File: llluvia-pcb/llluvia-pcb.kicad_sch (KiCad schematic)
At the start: 30 parts, among them J2 JACK_DC, J3 JACK_DC, J4 ON/OFF, J5 AudioJack, Q2 PN2222A, U1 LM324

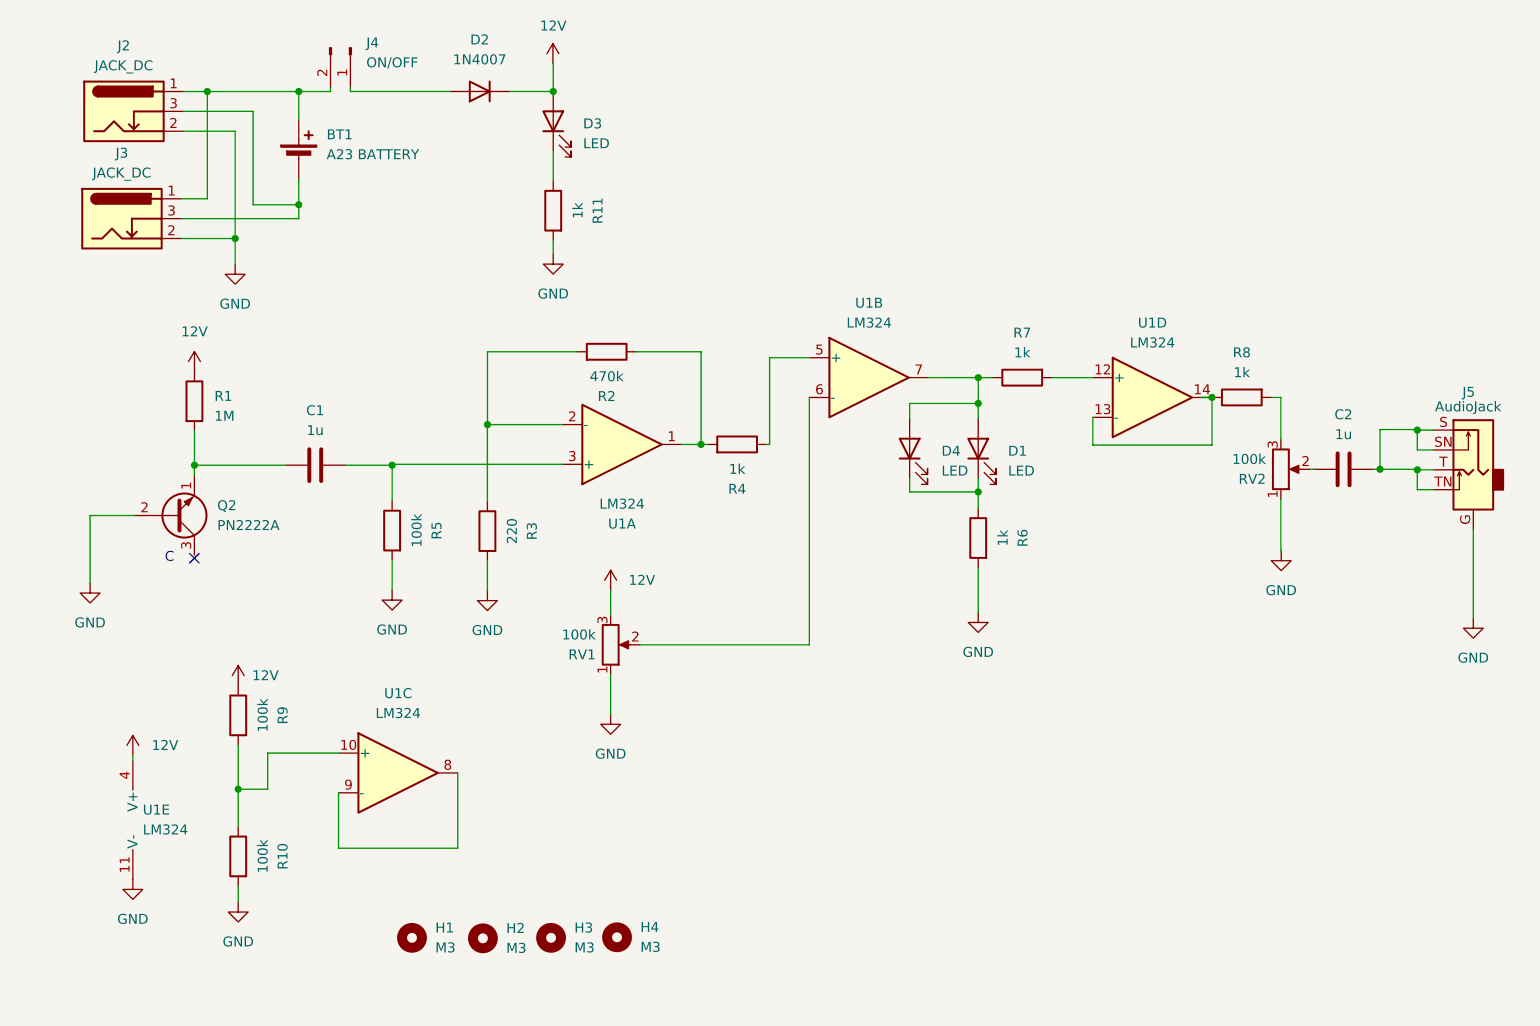
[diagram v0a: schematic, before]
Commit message: Esquemático rev 3: estabilizar etapa de ruido y comparador
- C3 (47u) en serie con R3: la ganancia DC de U1A baja de ~2137 a 1,
  así el offset y la corriente de bias del LM324 ya no lo saturan.
- R5 y extremo inferior de RV1 conectados a VREF (salida de U1C, que
  antes no iba a ningún lado). El ruido oscila alrededor de VREF y
  todo el recorrido de RV1 es útil.
- C4 (10u) en el divisor R9/R10 para filtrar VREF.
- C5 (100n) + C6 (47u) de desacople en el riel de 12V.
- R12 (100k, DNP) opcional: histéresis ~0,1 V en el comparador U1B.
- R11 1k -> 4.7k: el LED piloto pasa de ~9 mA a ~2 mA (batería A23).

El PCB no está actualizado: requiere Update PCB from Schematic y ruteo.

Co-Authored-By: Claude Opus 5.5 <noreply@anthropic.com>
Claude-Session: https://claude.ai/code/session_01RUaYEoGPN41cDPPqmjMNFH
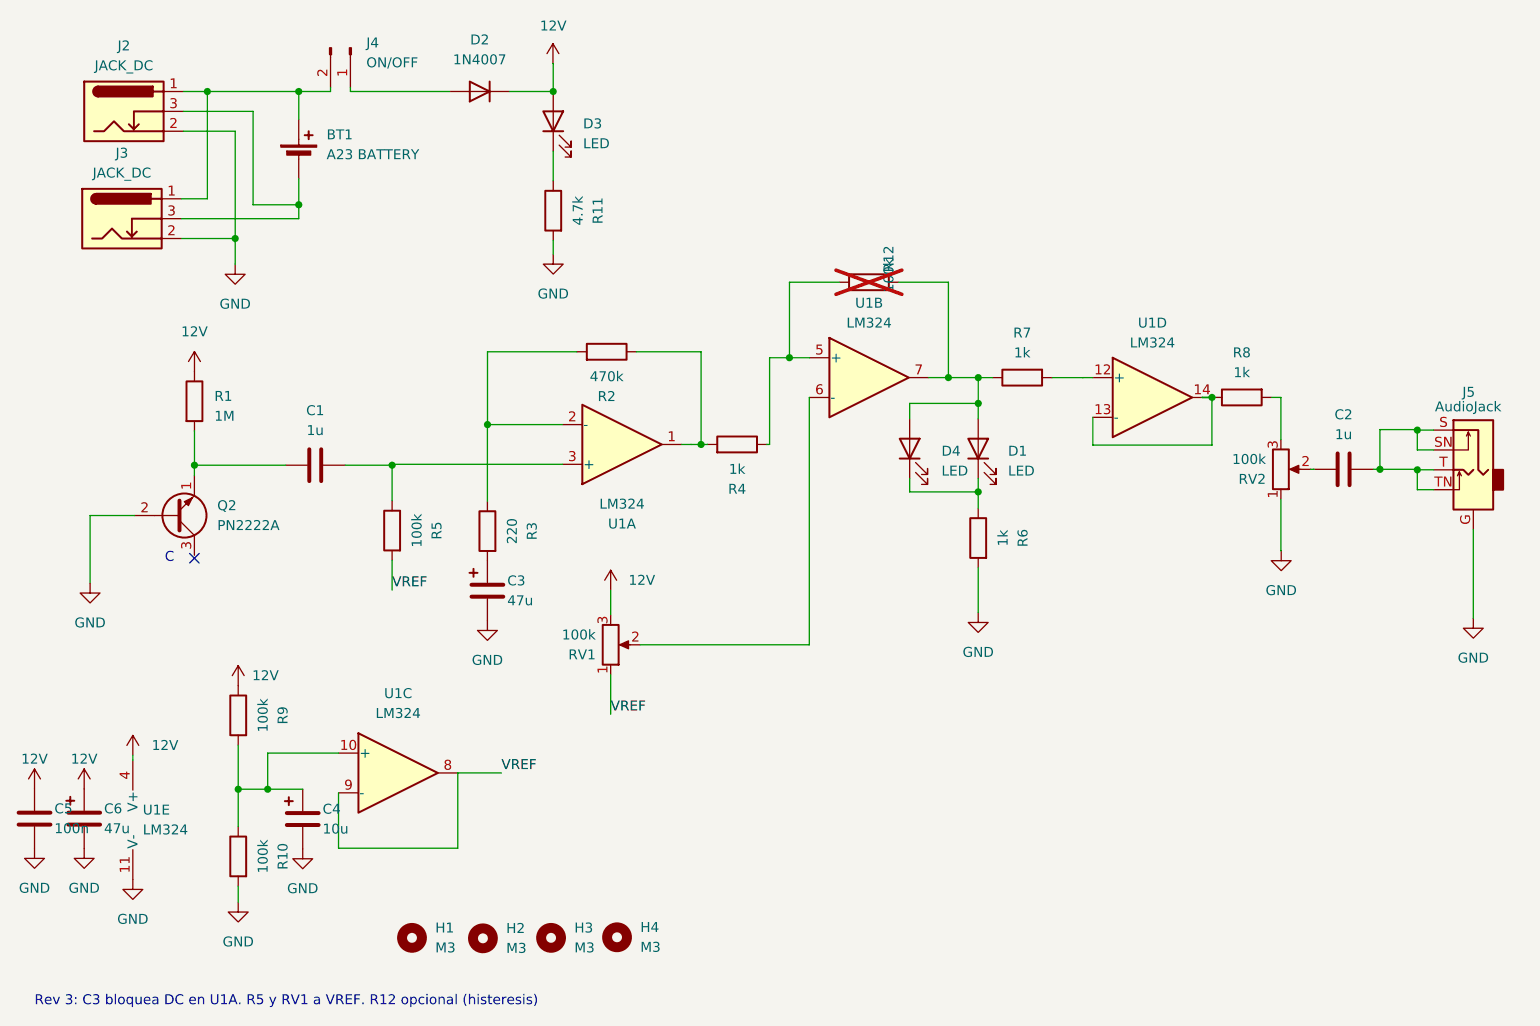
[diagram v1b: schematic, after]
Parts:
- added C3, C6: 47u, Capacitor_THT:CP_Radial_D5.0mm_P2.00mm, symbol Device:C_Polarized
- added C4: 10u, Capacitor_THT:CP_Radial_D5.0mm_P2.00mm, symbol Device:C_Polarized
- added C5: 100n, Capacitor_THT:C_Disc_D5.1mm_W3.2mm_P5.00mm, symbol Device:C
- added R12: 100k, Resistor_THT:R_Axial_DIN0207_L6.3mm_D2.5mm_P10.16mm_Horizontal, symbol Device:R
- R11: value 1k -> 4.7k
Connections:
- net 12V: now also C5.1, C6.1
- net GND: now also C3.2, C4.2, C5.2, C6.2; no longer R3.2, R5.2, RV1.1
- net at D1.2 (A), D4.2 (A), R7.1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: now also R12.2
- net at R10.1, R9.2, U1.10 (+): now also C4.1
- net at R4.1, U1.5 (+): now also R12.1
- net VREF: now reaches U1.8, U1.9 (-)
- net VREF: now also R5.2, RV1.1
- new net: C3.1, R3.2
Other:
- note added: "Rev 3: C3 bloquea DC en U1A. R5 y RV1 a VREF. R12 opcional (histeresis)"
